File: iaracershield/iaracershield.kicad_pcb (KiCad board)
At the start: 2 copper layers, 61 x 66 mm, 33 parts, among them J1 Conn_02x20_Odd_Even, J2 Conn_02x20_Odd_Even, Q1 DMG2305UX, SW1 PTS815 SJM 250 SMTR LFS, U1 DRV8835DSSR

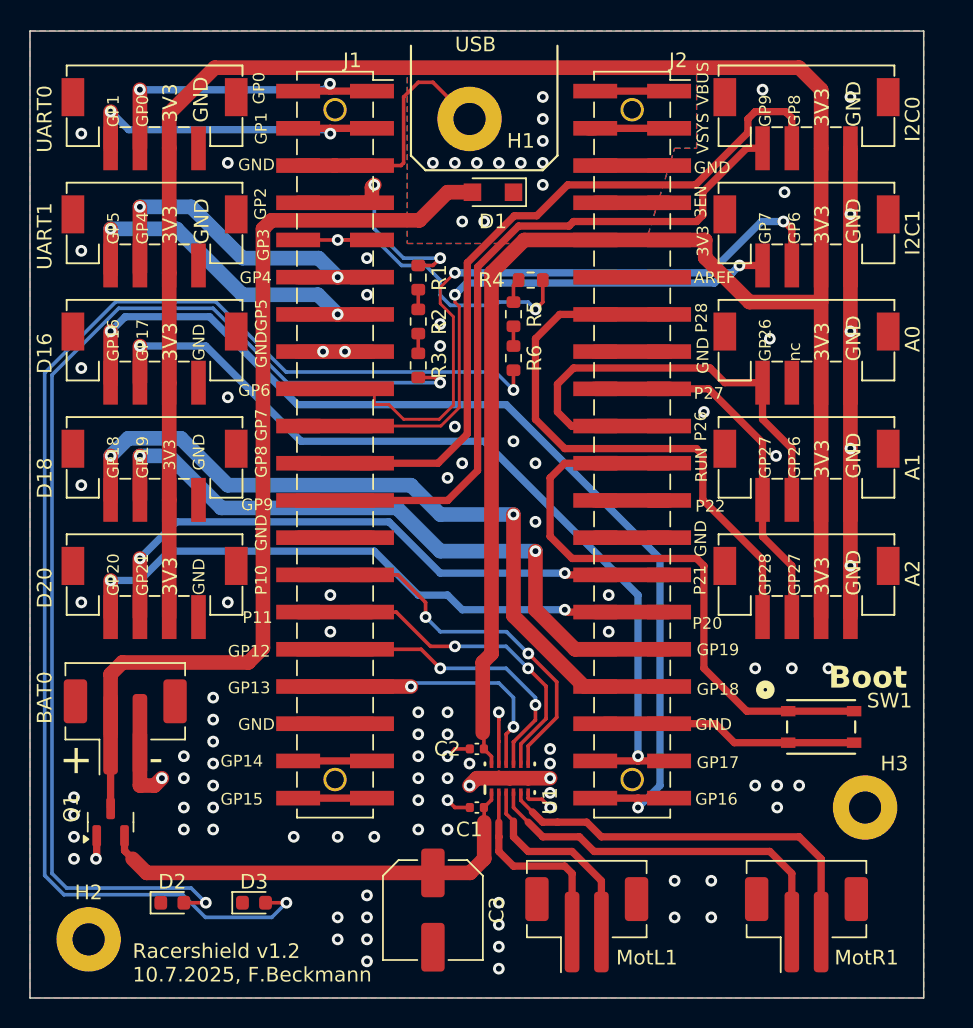
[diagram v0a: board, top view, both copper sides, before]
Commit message: cleanup: rename fredo to iaracershield, move production to iaracershield
I renamed all fredo names to iaracershield to have the same as for
ialed, iagabel and ialightsens. I also moved the production directory
to the iaracershield directory.
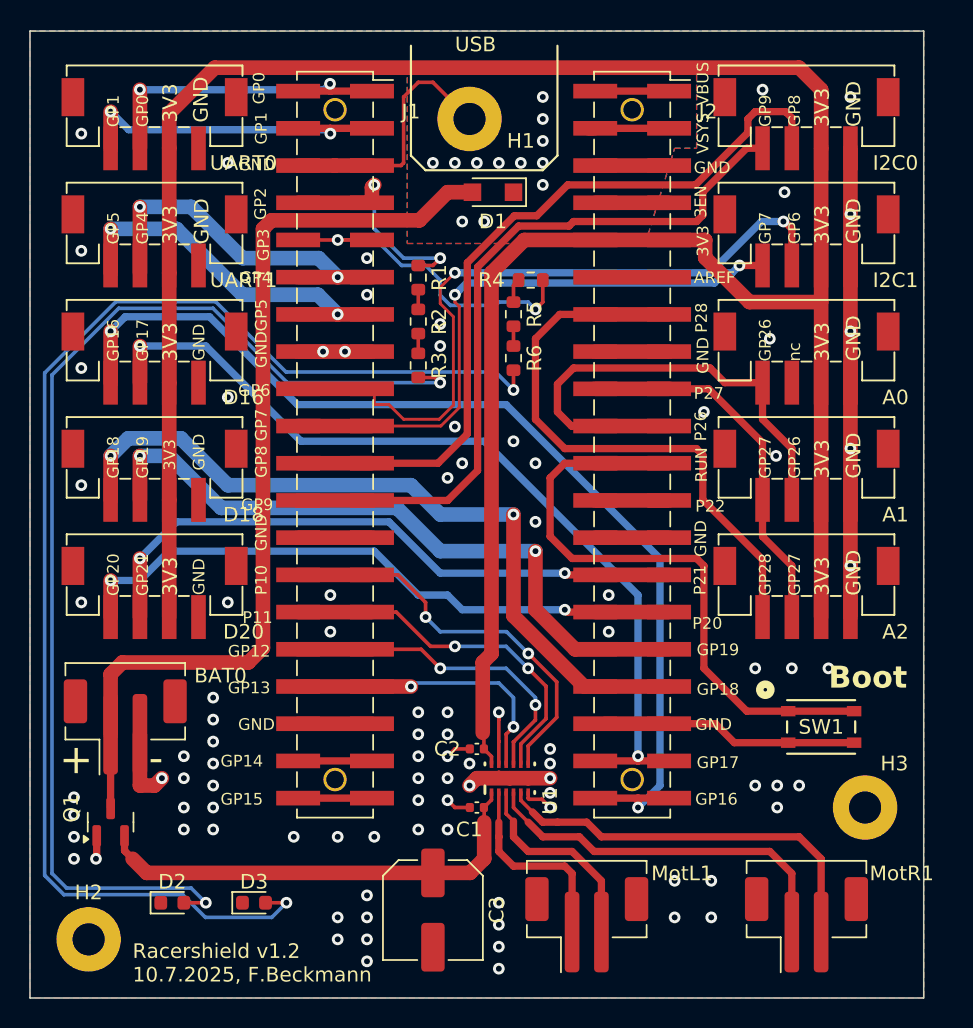
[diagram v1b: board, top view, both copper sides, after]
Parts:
- A0, A1, A2, D16, D18, D20, I2C0, I2C1, UART0, UART1: footprint fredo:GROVE-HW4-SMD-2.0 -> iaracershield:GROVE-HW4-SMD-2.0
- BAT0, MotL1, MotR1: footprint fredo:JST_PH_B2B-PH-SM4-TB_1x02-1MP_P2.00mm_Vertical -> iaracershield:JST_PH_B2B-PH-SM4-TB_1x02-1MP_P2.00mm_Vertical
- J1, J2: footprint fredo:PinSocket_2x20_P2.54mm_Vertical_SMD -> iaracershield:PinSocket_2x20_P2.54mm_Vertical_SMD
- SW1: footprint fredo:SW4_PTS815 SJM 250 SMTR LFS_CNK -> iaracershield:SW4_PTS815 SJM 250 SMTR LFS_CNK
- U1: footprint fredo:DSS0012A -> iaracershield:DSS0012A
